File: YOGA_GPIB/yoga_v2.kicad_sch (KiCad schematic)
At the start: 85 parts, among them J1 Conn_01x01_Female, J2 Conn_01x01_Female, J3 Conn_02x13_Odd_Even, J4 Conn_02x12_GPIB_PCB, J5 Raspberry_Pi_2_3, J6 Conn_01x10, J7 Conn_01x04, J8 22-23-2031, J9 Conn_01x05, Q1 BCW33, Q2 BCW30, Q3 BSS138, Q4 BSS138, U1 TPS62932, U2 LSF0108, U3 LSF0108, U4 24LC64, U5 ADM3202ARU, U6 SP385E

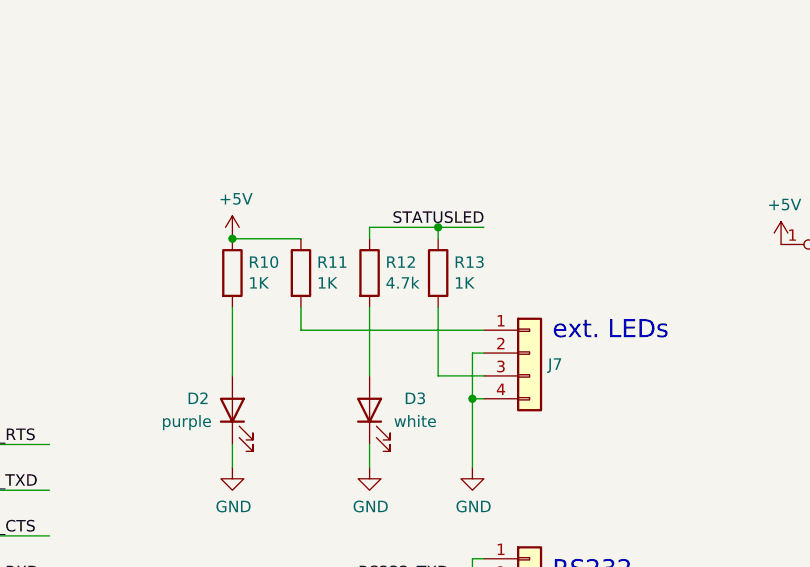
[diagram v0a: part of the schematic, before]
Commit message: YOGA_GPIB: update LED resistors and wiring documentation
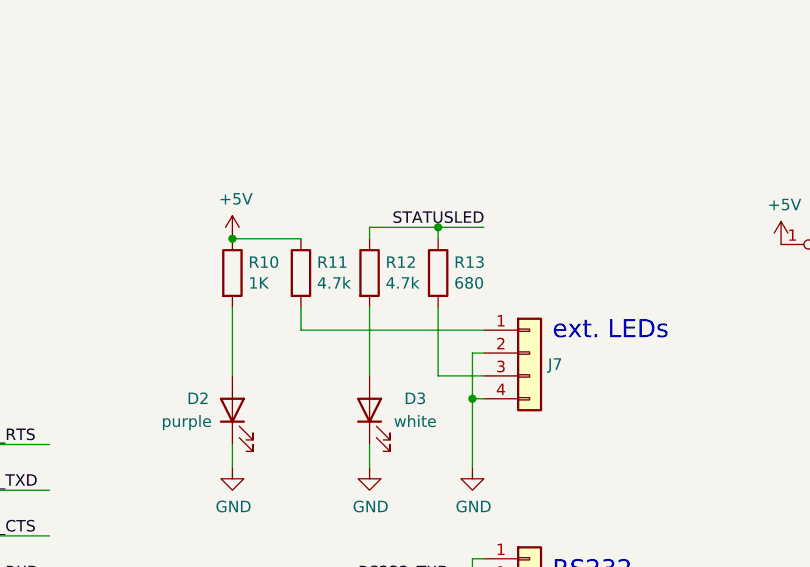
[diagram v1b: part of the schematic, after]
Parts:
- R11: value 1K -> 4.7k
- R13: value 1K -> 680
- R2: value 4.7 -> 4.7
